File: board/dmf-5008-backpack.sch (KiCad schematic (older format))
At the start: 5 parts, among them P1 CONN_01X25

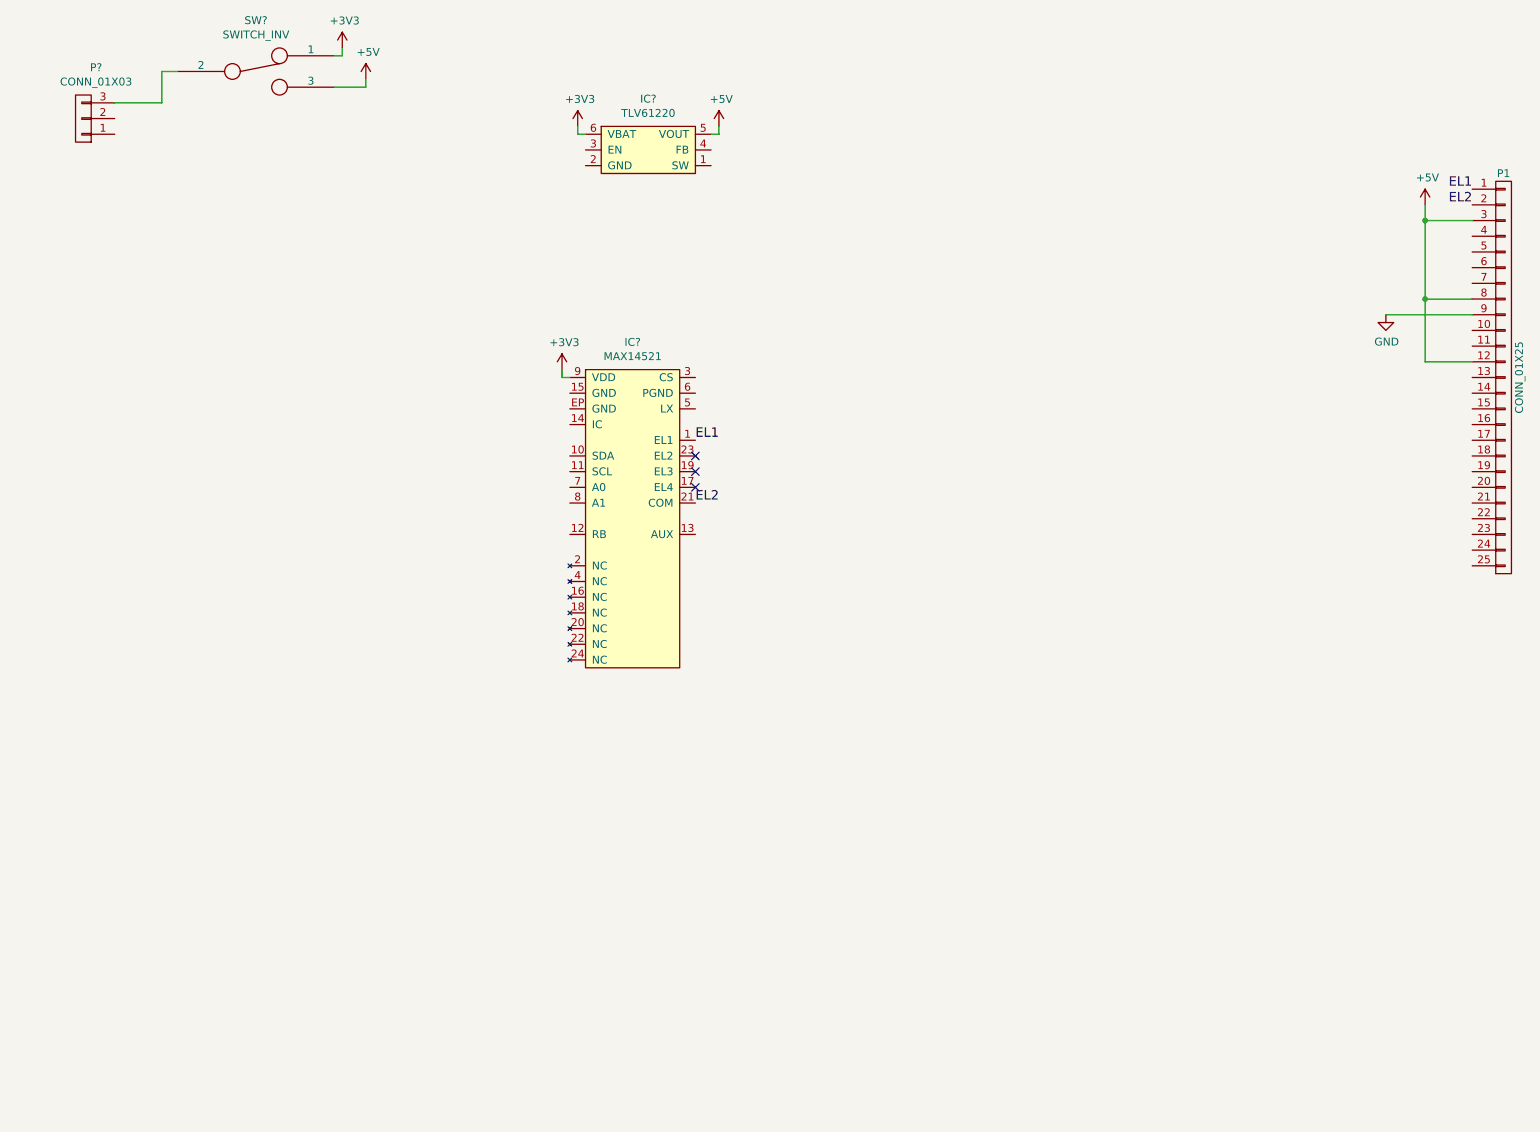
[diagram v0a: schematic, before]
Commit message: Change EL to simpler HV823 inverter
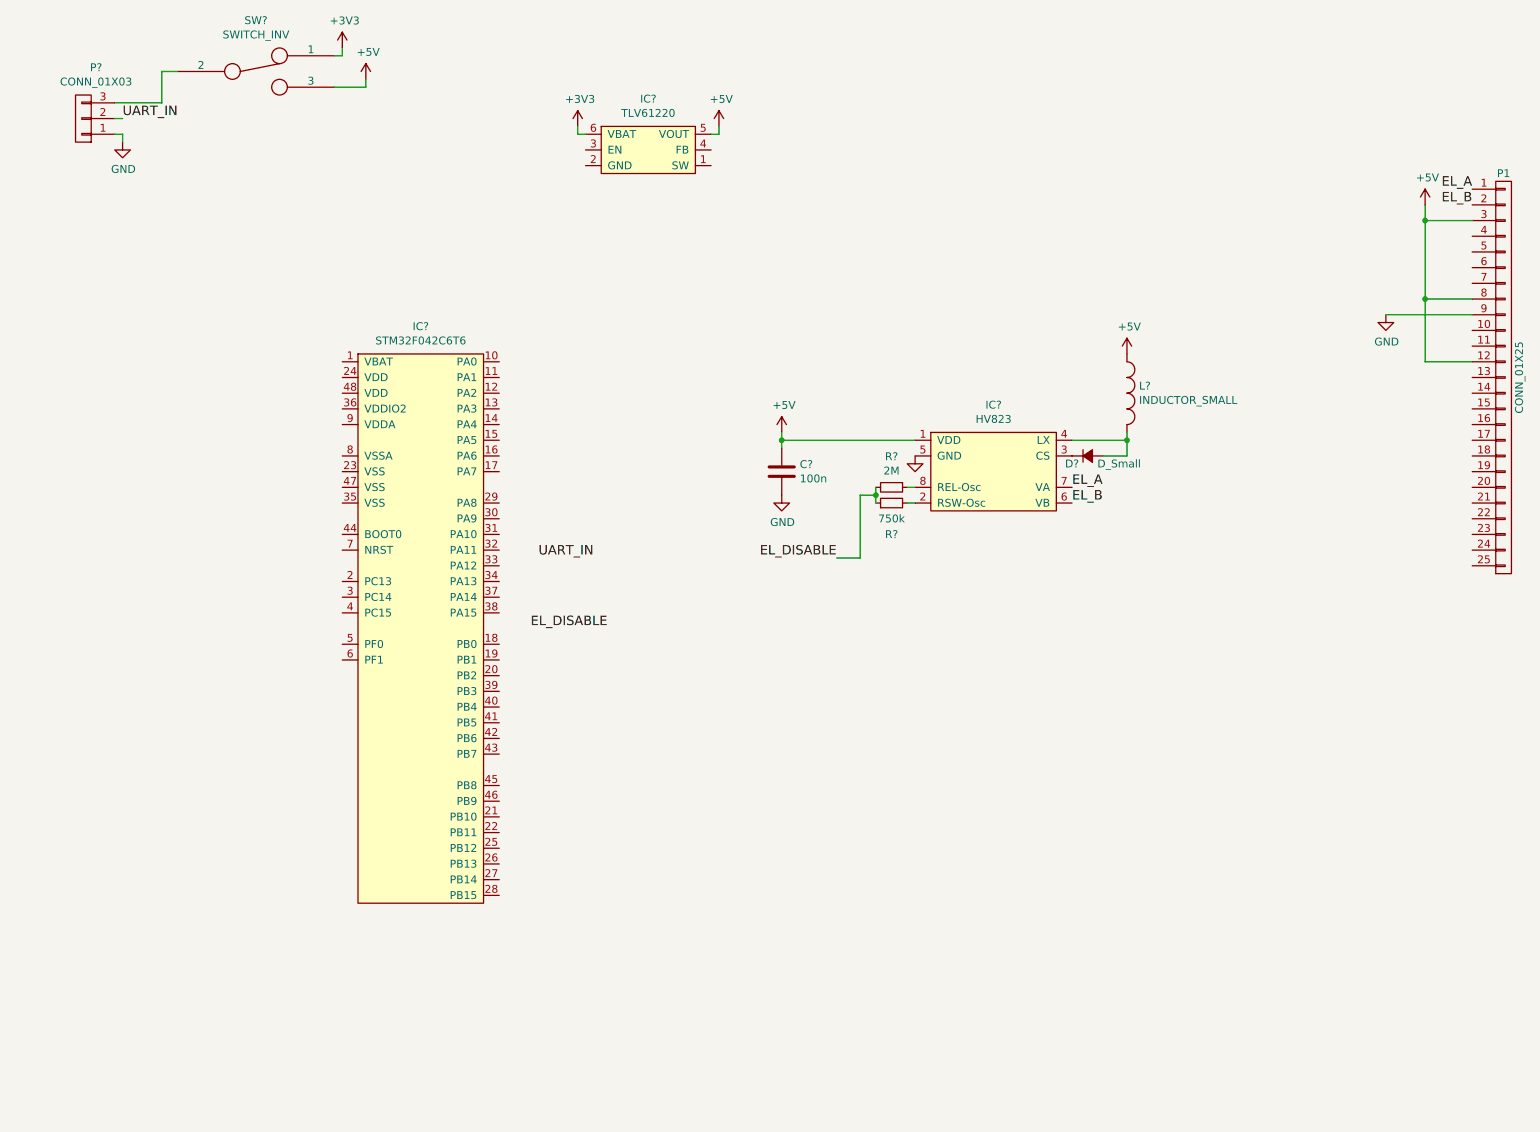
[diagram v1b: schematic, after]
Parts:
- removed IC?: MAX14521, agg:QFN-24-EP-MAX, symbol MAX14521
- added C?: 100n, symbol C
- added D?: D_Small, symbol D_Small
- added IC?: STM32F042C6T6, agg:LQFP-48, symbol STM32F0xxCxTx
- added IC?: HV823, agg:SOIC-8, symbol HV823
- added L?: INDUCTOR_SMALL, symbol INDUCTOR_SMALL
- added R?: 2M, symbol R_Small
- added R?: 750k, symbol R_Small
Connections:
- net +5V: now also C?.1, IC?.1 (VDD), L?.1
- net GND: now also P?.1 (P1), C?.2, IC?.5 (GND)
- net UART_IN: now reaches P?.2 (P2)
- net EL1 renamed EL_A
- net EL_A: now also IC?.7 (VA)
- net EL2 renamed EL_B
- net EL_B: now also IC?.6 (VB)
- new net: IC?.2 (RSW-Osc), R?.2
- new net: D?.1 (K), IC?.3 (CS)
- new net: D?.2 (A), IC?.4 (LX), L?.2
- new net: IC?.8 (REL-Osc), R?.1
- new net EL_DISABLE: R?.1, R?.2
- no-connect marks 3 -> 0
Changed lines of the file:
@@
 LIBS:contrib
 LIBS:valves
-LIBS:max14521
 LIBS:tlv61220
+LIBS:stm32f0xxcxtx
+LIBS:hv823
 LIBS:dmf-5008-backpack-cache
 EELAYER 26 0
@@
 $EndComp
 $Comp
-L MAX14521 IC?
-U 1 1 589CF444
-P 4900 3950
-F 0 "IC?" H 4900 5075 50  0000 C CNN
-F 1 "MAX14521" H 4900 4984 50  0000 C CNN
-F 2 "agg:QFN-24-EP-MAX" H -50 -1150 50  0001 L CNN
-F 3 "https://datasheets.maximintegrated.com/en/ds/MAX14521E.pdf" H -50 -1250 50  0001 L CNN
-F 4 "" H -50 -1350 50  0001 L CNN "Farnell"
-	1    4900 3950
-	1    0    0    -1
-$EndComp
-$Comp
 L TLV61220 IC?
 U 1 1 589CF8E1
@@
 Wire Wire Line
 	5450 1500 5400 1500
-$Comp
-L +3V3 #PWR?
-U 1 1 589CFBC0
-P 4450 3000
-F 0 "#PWR?" H 450 100 50  0001 C CNN
-F 1 "+3V3" H 4465 3173 50  0000 C CNN
-F 2 "" H 450 250 50  0000 C CNN
-F 3 "" H 450 250 50  0000 C CNN
-	1    4450 3000
-	1    0    0    -1
-$EndComp
-Wire Wire Line
-	4450 3000 4450 3050
-Wire Wire Line
-	4450 3050 4500 3050
 Text Label 10250 1850 2    60   ~ 0
-EL1
+EL_A
 Text Label 10250 1950 2    60   ~ 0
-EL2
-Text Label 5300 3450 0    60   ~ 0
-EL1
-Text Label 5300 3850 0    60   ~ 0
-EL2
-NoConn ~ 5300 3550
-NoConn ~ 5300 3650
-NoConn ~ 5300 3750
+EL_B
 $Comp
 L +5V #PWR?
@@
 	9950 2950 10250 2950
 Connection ~ 9950 2550
+$Comp
+L STM32F0xxCxTx IC?
+U 1 1 589F4142
+P 3550 4650
+F 0 "IC?" H 3550 6575 50  0000 C CNN
+F 1 "STM32F042C6T6" H 3550 6484 50  0000 C CNN
+F 2 "agg:LQFP-48" H -400 -1400 50  0001 L CNN
+F 3 "http://www.st.com/resource/en/datasheet/stm32f042c6.pdf" H -400 -1500 50  0001 L CNN
+F 4 "110-6612" H 3550 4650 60  0001 C CNN "RS"
+	1    3550 4650
+	1    0    0    -1
+$EndComp
+$Comp
+L GND #PWR?
+U 1 1 58A2450D
+P 1650 1550
+F 0 "#PWR?" H -200 -200 50  0001 C CNN
+F 1 "GND" H 1655 1377 50  0000 C CNN
+F 2 "" H -200 50  50  0000 C CNN
+F 3 "" H -200 50  50  0000 C CNN
+	1    1650 1550
+	1    0    0    -1
+$EndComp
+Wire Wire Line
+	1650 1550 1650 1500
+Wire Wire Line
+	1650 1500 1600 1500
+Text Label 1650 1400 0    60   ~ 0
+UART_IN
+Wire Wire Line
+	1650 1400 1600 1400
+Text Label 4300 4200 0    60   ~ 0
+UART_IN
+Text Label 4250 4650 0    60   ~ 0
+EL_DISABLE
+$Comp
+L HV823 IC?
+U 1 1 58A62E88
+P 7200 3650
+F 0 "IC?" H 7200 4075 50  0000 C CNN
+F 1 "HV823" H 7200 3984 50  0000 C CNN
+F 2 "agg:SOIC-8" H -200 -750 50  0001 L CNN
+F 3 "http://ww1.microchip.com/downloads/en/DeviceDoc/HV823%20C082213.pdf" H -200 -850 50  0001 L CNN
+	1    7200 3650
+	1    0    0    -1
+$EndComp
+$Comp
+L +5V #PWR?
+U 1 1 58A62F84
+P 5850 3400
+F 0 "#PWR?" H 5900 3450 50  0001 C CNN
+F 1 "+5V" H 5865 3573 50  0000 C CNN
+F 2 "" H -1200 -250 50  0000 C CNN
+F 3 "" H -1200 -250 50  0000 C CNN
+	1    5850 3400
+	1    0    0    -1
+$EndComp
+$Comp
+L C C?
+U 1 1 58A62FAA
+P 5850 3650
+F 0 "C?" H 5965 3696 50  0000 L CNN
+F 1 "100n" H 5965 3605 50  0000 L CNN
+F 2 "" H -162 150 50  0000 C CNN
+F 3 "" H -200 300 50  0000 C CNN
+	1    5850 3650
+	1    0    0    -1
+$EndComp
+Wire Wire Line
+	5850 3400 5850 3500
+Wire Wire Line
+	5850 3450 6700 3450
+Connection ~ 5850 3450
+$Comp
+L GND #PWR?
+U 1 1 58A63041
+P 5850 3800
+F 0 "#PWR?" H 5900 3850 50  0001 C CNN
+F 1 "GND" H 5855 3627 50  0000 C CNN
+F 2 "" H -200 -100 50  0000 C CNN
+F 3 "" H -200 -100 50  0000 C CNN
+	1    5850 3800
+	1    0    0    -1
+$EndComp
+$Comp
+L R_Small R?
+U 1 1 58A630A2
+P 6550 3750
+F 0 "R?" V 6354 3750 50  0000 C CNN
+F 1 "2M" V 6445 3750 50  0000 C CNN
+F 2 "" H 350 -250 50  0000 C CNN
+F 3 "" H 350 -250 50  0000 C CNN
+	1    6550 3750
+	0    1    1    0
+$EndComp
+$Comp
+L R_Small R?
+U 1 1 58A6314C
+P 6550 3850
+F 0 "R?" V 6350 3850 50  0000 C CNN
+F 1 "750k" V 6450 3850 50  0000 C CNN
+F 2 "" H 150 -100 50  0000 C CNN
+F 3 "" H 150 -100 50  0000 C CNN
+	1    6550 3850
+	0    -1   -1   0
+$EndComp
+Wire Wire Line
+	6450 3750 6450 3850
+Text Label 6200 4200 2    60   ~ 0
+EL_DISABLE
+Wire Wire Line
+	6200 4200 6350 4200
+Wire Wire Line
+	6350 4200 6350 3800
+Wire Wire Line
+	6350 3800 6450 3800
+Connection ~ 6450 3800
+$Comp
+L GND #PWR?
+U 1 1 58A6395F
+P 6700 3550
+F 0 "#PWR?" H 6750 3600 50  0001 C CNN
+F 1 "GND" H 6705 3377 50  0001 C CNN
+F 2 "" H -350 -50 50  0000 C CNN
+F 3 "" H -350 -50 50  0000 C CNN
+	1    6700 3550
+	1    0    0    -1
+$EndComp
+Wire Wire Line
+	6650 3750 6700 3750
+Wire Wire Line
+	6700 3850 6650 3850
+$Comp
+L INDUCTOR_SMALL L?
+U 1 1 58A63DBE
+P 8050 3150
+F 0 "L?" V 8004 3227 50  0000 L CNN
+F 1 "INDUCTOR_SMALL" V 8095 3227 50  0000 L CNN
+F 2 "" H 150 -100 50  0000 C CNN
+F 3 "" H 150 -100 50  0000 C CNN
+	1    8050 3150
+	0    1    1    0
+$EndComp
+Wire Wire Line
+	7700 3450 8050 3450
+$Comp
+L +5V #PWR?
+U 1 1 58A6416F
+P 8050 2900
+F 0 "#PWR?" H 8100 2950 50  0001 C CNN
+F 1 "+5V" H 8065 3073 50  0000 C CNN
+F 2 "" H 700 100 50  0000 C CNN
+F 3 "" H 700 100 50  0000 C CNN
+	1    8050 2900
+	1    0    0    -1
+$EndComp
+$Comp
+L D_Small D?
+U 1 1 58A64241
+P 7800 3550
+F 0 "D?" H 7700 3500 50  0000 C CNN
+F 1 "D_Small" H 8000 3500 50  0000 C CNN
+F 2 "" V -100 150 50  0000 C CNN
+F 3 "" V -100 150 50  0000 C CNN
+	1    7800 3550
+	1    0    0    -1
+$EndComp
+Wire Wire Line
+	8050 3400 8050 3550
+Wire Wire Line
+	8050 3550 7900 3550
+Connection ~ 8050 3450
+Text Label 7700 3750 0    60   ~ 0
+EL_A
+Text Label 7700 3850 0    60   ~ 0
+EL_B
 $EndSCHEMATC

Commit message: filled in more circuit
Did most STM32 support, LCD lines, step-up converter
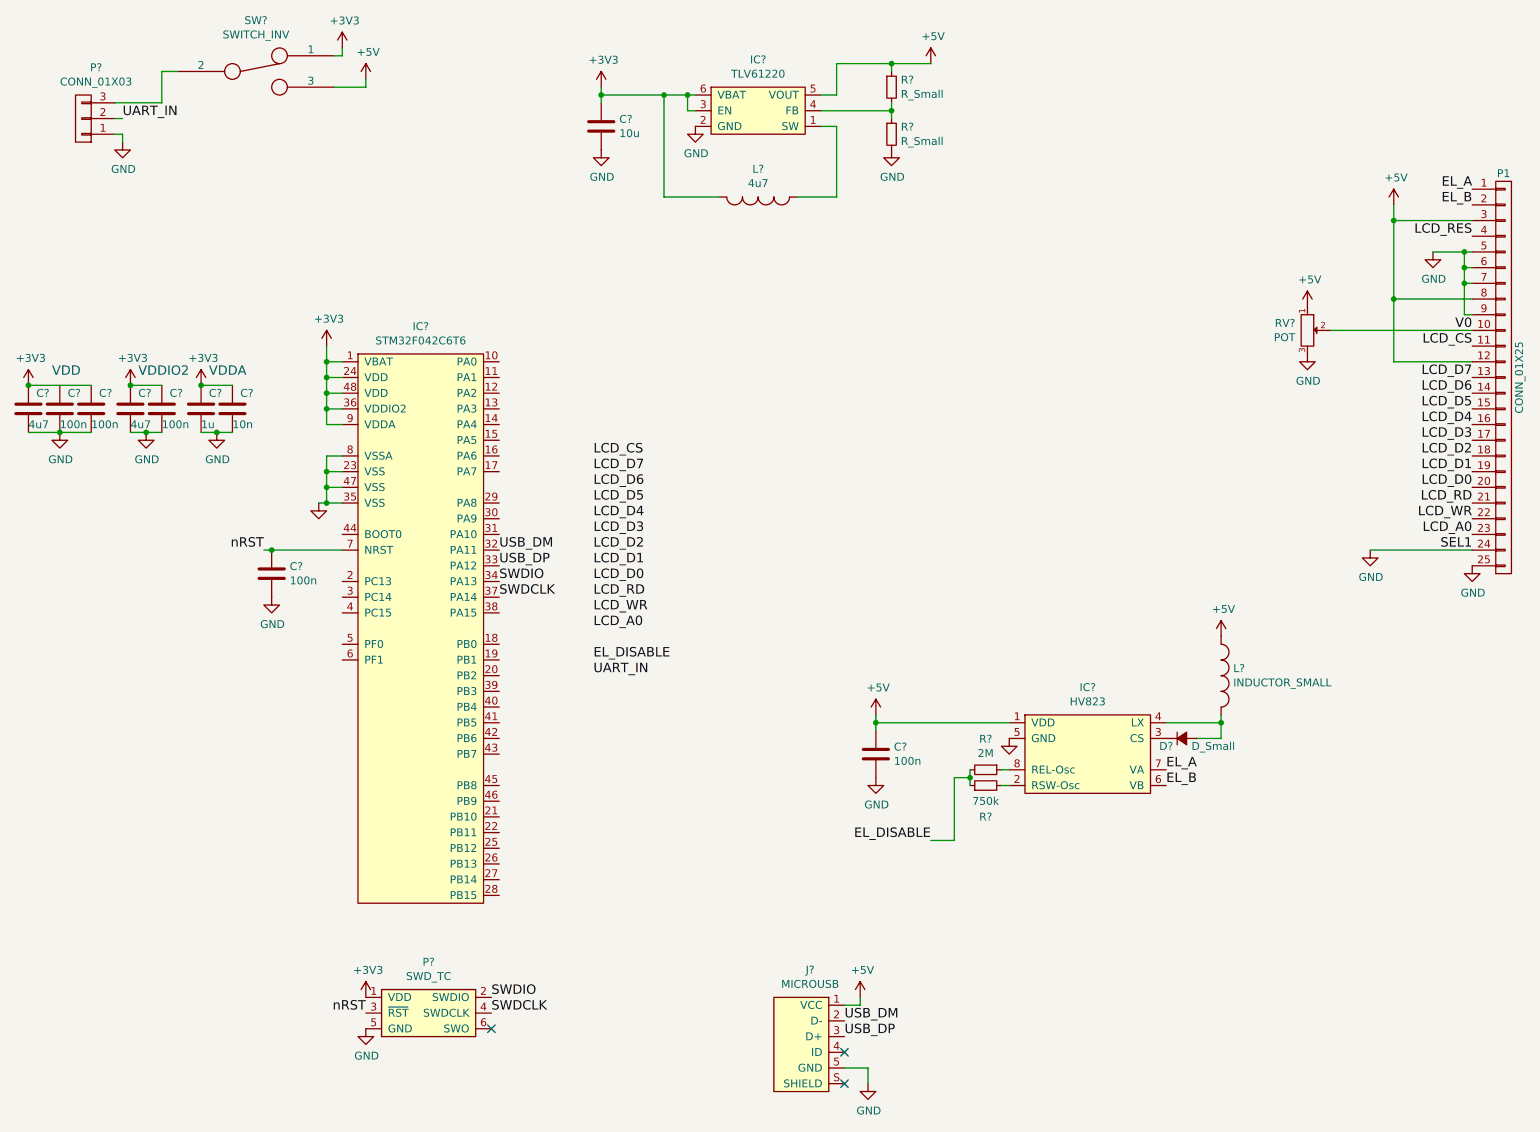
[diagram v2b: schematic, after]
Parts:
- added C?: 10u, symbol C
- added C? (x2): 4u7, symbol C
- added C? (x4): 100n, symbol C
- added C?: 1u, symbol C
- added C?: 10n, symbol C
- added J?: MICROUSB, agg:MICROUSB_MOLEX_47589-0001, symbol MICROUSB
- added L?: 4u7, symbol INDUCTOR_SMALL
- added P?: SWD_TC, agg:TC2030-NL, symbol SWD_TC
- added R? (x2): R_Small, symbol R_Small
- added RV?: POT, symbol POT
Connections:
- net +3V3: now also IC?.1 (VBAT), IC?.24 (VDD), IC?.3 (EN), IC?.36 (VDDIO2), IC?.48 (VDD), IC?.9 (VDDA), C?.1, C?.1, C?.1, C?.1, C?.1, C?.1, C?.1, L?.2, P?.1 (VDD)
- net +5V: now also J?.1 (VCC), R?.1, RV?.1
- net GND: now also IC?.2 (GND), IC?.23 (VSS), IC?.35 (VSS), IC?.47 (VSS), IC?.8 (VSSA), P1.24 (P24), P1.25 (P25), P1.5 (P5), P1.6 (P6), P1.7 (P7), C?.2, C?.2, C?.2, C?.2, C?.2, C?.2, C?.2, C?.2, C?.2, J?.5 (GND), P?.5 (GND), R?.2, RV?.3
- net V0: now reaches P1.10 (P10)
- net V0: now also RV?.2
- net LCD_CS: now reaches P1.11 (P11)
- net LCD_D7: now reaches P1.13 (P13)
- net LCD_D6: now reaches P1.14 (P14)
- net LCD_D5: now reaches P1.15 (P15)
- net LCD_D4: now reaches P1.16 (P16)
- net LCD_D3: now reaches P1.17 (P17)
- net LCD_D2: now reaches P1.18 (P18)
- net LCD_D1: now reaches P1.19 (P19)
- net LCD_D0: now reaches P1.20 (P20)
- net LCD_RD: now reaches P1.21 (P21)
- net LCD_WR: now reaches P1.22 (P22)
- net LCD_A0: now reaches P1.23 (P23)
- net LCD_RES: now reaches P1.4 (P4)
- net at IC?.1 (SW): now also L?.1
- net at IC?.4 (FB): now also R?.1, R?.2
- net USB_DM: now reaches IC?.32 (PA11)
- net USB_DM: now also J?.2 (D-)
- net USB_DP: now reaches IC?.33 (PA12)
- net USB_DP: now also J?.3 (D+)
- net SWDIO: now reaches IC?.34 (PA13)
- net SWDIO: now also P?.2 (SWDIO)
- net SWDCLK: now reaches IC?.37 (PA14)
- net SWDCLK: now also P?.4 (SWDCLK)
- net nRST: now reaches IC?.7 (NRST)
- net nRST: now also C?.1, P?.3 (~RST)
- no-connect marks 0 -> 3
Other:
- note added: "VDD"
- note added: "VDDA"
- note added: "VDDIO2"
- moved on the sheet: C?, D?, IC?, L?, R?

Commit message: footprints
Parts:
- removed C? (x2): 100n, symbol C
- removed C?: 4u7, symbol C
- added C?: 4u7, agg:0805, symbol C
- C?: footprint (none) -> agg:0805; Farnell (none) -> 1759420
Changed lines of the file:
@@
 F 0 "C?" H 1100 3350 50  0000 L CNN
 F 1 "4u7" H 1050 3150 50  0000 L CNN
-F 2 "" H -862 100 50  0000 C CNN
+F 2 "agg:0805" H -862 100 50  0001 C CNN
 F 3 "" H -900 250 50  0000 C CNN
+F 4 "1759420" H 1050 3250 60  0001 C CNN "Farnell"
 	1    1050 3250
 	1    0    0    -1
@@
 F 3 "" H -700 250 50  0000 C CNN
 	1    1250 3250
-	1    0    0    -1
-$EndComp
-$Comp
-L C C?
-U 1 1 58A679BB
-P 1450 3250
-F 0 "C?" H 1500 3350 50  0000 L CNN
-F 1 "100n" H 1450 3150 50  0000 L CNN
-F 2 "" H -462 100 50  0000 C CNN
-F 3 "" H -500 250 50  0000 C CNN
-	1    1450 3250
-	1    0    0    -1
-$EndComp
-$Comp
-L C C?
-U 1 1 58A67DCC
-P 1700 3250
-F 0 "C?" H 1750 3350 50  0000 L CNN
-F 1 "4u7" H 1700 3150 50  0000 L CNN
-F 2 "" H -212 100 50  0000 C CNN
-F 3 "" H -250 250 50  0000 C CNN
-	1    1700 3250
-	1    0    0    -1
-$EndComp
-$Comp
-L C C?
-U 1 1 58A67E16
-P 1900 3250
-F 0 "C?" H 1950 3350 50  0000 L CNN
-F 1 "100n" H 1900 3150 50  0000 L CNN
-F 2 "" H -12 100 50  0000 C CNN
-F 3 "" H -50 250 50  0000 C CNN
-	1    1900 3250
 	1    0    0    -1
 $EndComp
@@
 	1    0    0    -1
 $EndComp
+$Comp
+L C C?
+U 1 1 58A77375
+P 1700 3250
+F 0 "C?" H 1750 3350 50  0000 L CNN
+F 1 "4u7" H 1700 3150 50  0000 L CNN
+F 2 "agg:0805" H -212 100 50  0001 C CNN
+F 3 "" H -250 250 50  0000 C CNN
+F 4 "1759420" H 1700 3250 60  0001 C CNN "Farnell"
+	1    1700 3250
+	1    0    0    -1
+$EndComp
